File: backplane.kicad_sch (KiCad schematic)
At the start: 2 parts, among them J1 09031967921, U1 TPD2E2U06DCK

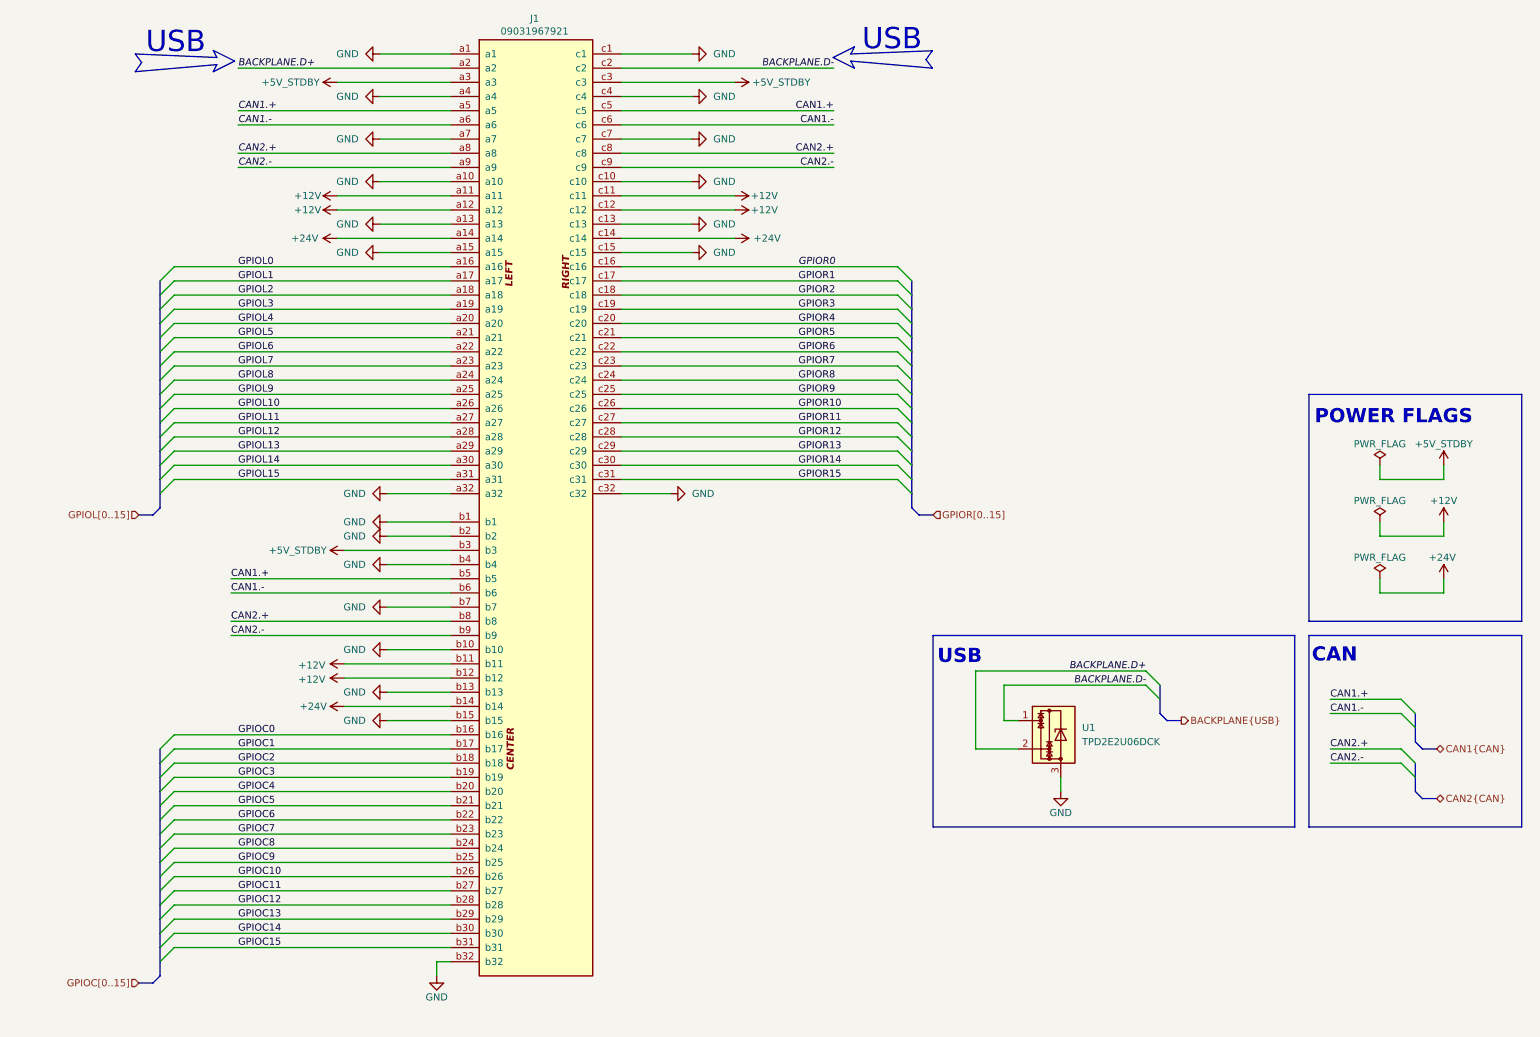
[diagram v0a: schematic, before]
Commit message: [#1] WIP: Change components to ones from the global library, refactor schematic
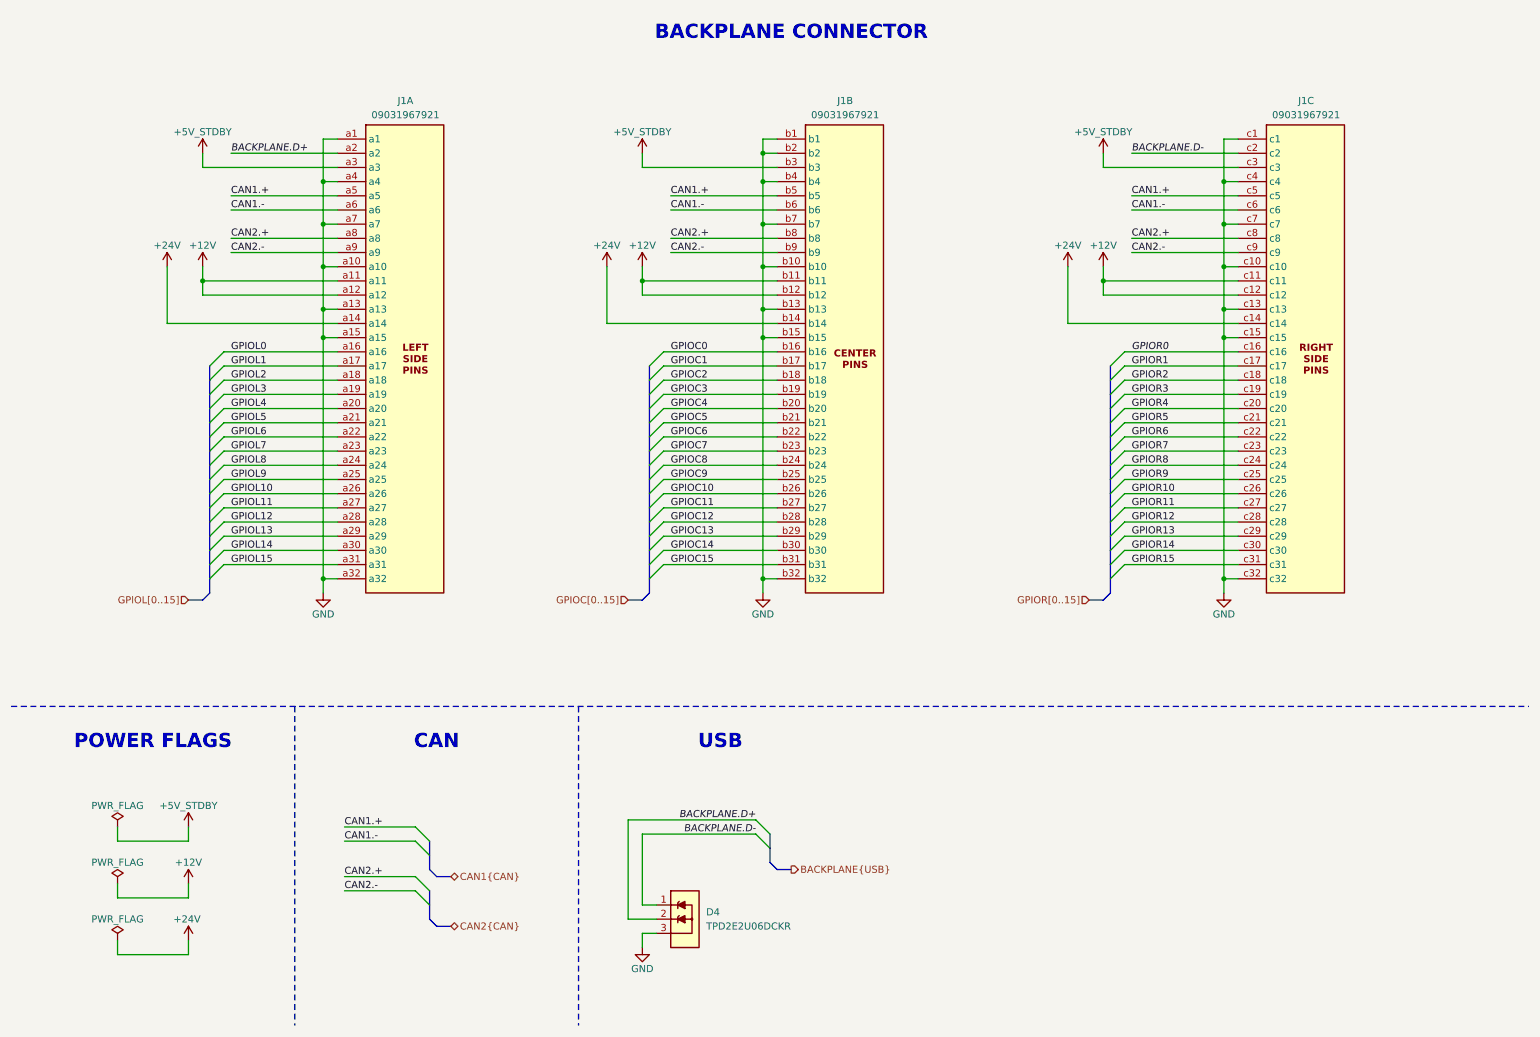
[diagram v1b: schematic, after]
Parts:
- removed J1: 09031967921, Connector_DIN:DIN41612_R_3x32_Female_Horizontal_THT, symbol DIN41612_3x32:09031967921
- removed U1: TPD2E2U06DCK, Package_TO_SOT_SMD:SOT-323_SC-70, symbol Power_Protection:TPD2E2U06DCK
- added D4: TPD2E2U06DCKR, DW-footprints:SOT-323, symbol DW-TVS:TPD2E2U06DCKR
- added J1: DIN-41612-connector_09031967921, DW-footprints:DIN-41612-connector_09031967921, symbol DW-connectors:DIN-41612-connector_09031967921
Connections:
- net +12V: now also J1.a11, J1.a12, J1.b11, J1.b12, J1.c11, J1.c12
- net +24V: now also J1.a14, J1.b14, J1.c14
- net +5V_STDBY: now also J1.a3, J1.b3, J1.c3
- net BACKPLANE.D+: now also D4.2, J1.a2
- net BACKPLANE.D-: now also D4.1, J1.c2
- net CAN1.+: now also J1.a5, J1.b5, J1.c5
- net CAN1.-: now also J1.a6, J1.b6, J1.c6
- net CAN2.+: now also J1.a8, J1.b8, J1.c8
- net CAN2.-: now also J1.a9, J1.b9, J1.c9
- net GND: now also D4.3, J1.a1, J1.a10, J1.a13, J1.a15, J1.a32, J1.a4, J1.a7, J1.b1, J1.b10, J1.b13, J1.b15, J1.b2, J1.b32, J1.b4, J1.b7, J1.c1, J1.c10, J1.c13, J1.c15, J1.c32, J1.c4, J1.c7
- net GPIOC0: now also J1.b16
- net GPIOC1: now also J1.b17
- net GPIOC10: now also J1.b26
- net GPIOC11: now also J1.b27
- net GPIOC12: now also J1.b28
- net GPIOC13: now also J1.b29
- net GPIOC14: now also J1.b30
- net GPIOC15: now also J1.b31
- net GPIOC2: now also J1.b18
- net GPIOC3: now also J1.b19
- net GPIOC4: now also J1.b20
- net GPIOC5: now also J1.b21
- net GPIOC6: now also J1.b22
- net GPIOC7: now also J1.b23
- net GPIOC8: now also J1.b24
- net GPIOC9: now also J1.b25
- net GPIOL0: now also J1.a16
- net GPIOL1: now also J1.a17
- net GPIOL10: now also J1.a26
- net GPIOL11: now also J1.a27
- net GPIOL12: now also J1.a28
- net GPIOL13: now also J1.a29
- net GPIOL14: now also J1.a30
- net GPIOL15: now also J1.a31
- net GPIOL2: now also J1.a18
- net GPIOL3: now also J1.a19
- net GPIOL4: now also J1.a20
- net GPIOL5: now also J1.a21
- net GPIOL6: now also J1.a22
- net GPIOL7: now also J1.a23
- net GPIOL8: now also J1.a24
- net GPIOL9: now also J1.a25
- net GPIOR0: now also J1.c16
- net GPIOR1: now also J1.c17
- net GPIOR10: now also J1.c26
- net GPIOR11: now also J1.c27
- net GPIOR12: now also J1.c28
- net GPIOR13: now also J1.c29
- net GPIOR14: now also J1.c30
- net GPIOR15: now also J1.c31
- net GPIOR2: now also J1.c18
- net GPIOR3: now also J1.c19
- net GPIOR4: now also J1.c20
- net GPIOR5: now also J1.c21
- net GPIOR6: now also J1.c22
- net GPIOR7: now also J1.c23
- net GPIOR8: now also J1.c24
- net GPIOR9: now also J1.c25
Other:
- note added: "BACKPLANE CONNECTOR"
